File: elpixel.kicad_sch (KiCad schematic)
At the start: 5 parts, among them J1 Conn_01x02, J2 Conn_01x04, Q1 BC857, U1 MC78M05_TO252, U2 WS2811

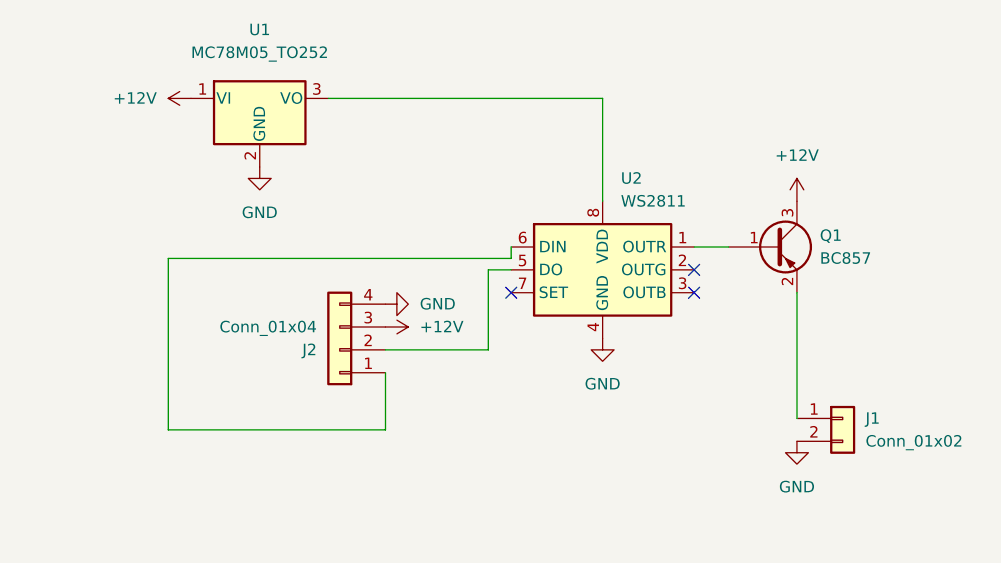
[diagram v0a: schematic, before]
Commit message: new version with different input/output pins to make the external wiring easier
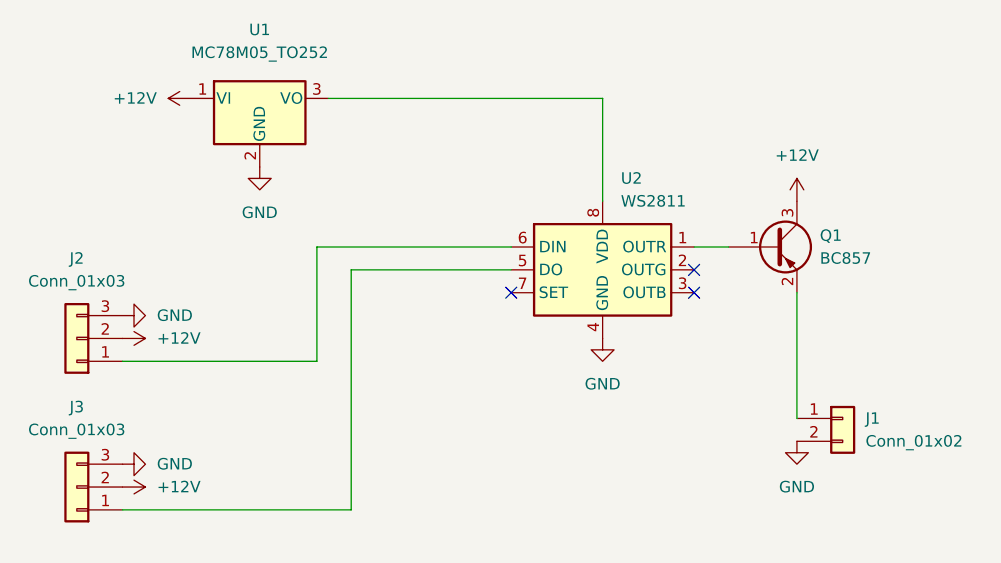
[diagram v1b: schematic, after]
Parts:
- removed J2: Conn_01x04, Connector_PinHeader_1.00mm:PinHeader_1x04_P1.00mm_Vertical, symbol Connector_Generic:Conn_01x04
- added J2, J3: Conn_01x03, Connector_PinHeader_1.00mm:PinHeader_1x03_P1.00mm_Vertical, symbol Connector_Generic:Conn_01x03
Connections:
- net +12V: now also J2.2 (Pin_2), J3.2 (Pin_2)
- net GND: now also J2.3 (Pin_3), J3.3 (Pin_3)
- net at U2.6 (DIN): now also J2.1 (Pin_1)
- net at U2.5 (DO): now also J3.1 (Pin_1)
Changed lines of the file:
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@@
   (no_connect (at 154.94 107.95))
   (no_connect (at 134.62 107.95))
+  (wire (pts (xy 134.62 105.41) (xy 116.84 105.41))
+    (stroke (width 0) (type default) (color 0 0 0 0))
+  )
+  (wire (pts (xy 116.84 105.41) (xy 116.84 132.08))
+    (stroke (width 0) (type default) (color 0 0 0 0))
+  )
   (wire (pts (xy 166.37 107.95) (xy 166.37 121.92))
     (stroke (width 0) (type default) (color 0 0 0 0))
@@
     (stroke (width 0) (type default) (color 0 0 0 0))
   )
-  (wire (pts (xy 96.52 123.19) (xy 96.52 104.14))
-    (stroke (width 0) (type default) (color 0 0 0 0))
-  )
-  (wire (pts (xy 120.65 116.84) (xy 120.65 123.19))
-    (stroke (width 0) (type default) (color 0 0 0 0))
-  )
-  (wire (pts (xy 132.08 105.41) (xy 134.62 105.41))
+  (wire (pts (xy 116.84 132.08) (xy 91.44 132.08))
     (stroke (width 0) (type default) (color 0 0 0 0))
   )
@@
     (stroke (width 0) (type default) (color 0 0 0 0))
   )
-  (wire (pts (xy 132.08 105.41) (xy 132.08 114.3))
-    (stroke (width 0) (type default) (color 0 0 0 0))
-  )
-  (wire (pts (xy 134.62 104.14) (xy 134.62 102.87))
-    (stroke (width 0) (type default) (color 0 0 0 0))
-  )
-  (wire (pts (xy 96.52 104.14) (xy 134.62 104.14))
-    (stroke (width 0) (type default) (color 0 0 0 0))
-  )
-  (wire (pts (xy 120.65 114.3) (xy 132.08 114.3))
-    (stroke (width 0) (type default) (color 0 0 0 0))
-  )
-  (wire (pts (xy 120.65 123.19) (xy 96.52 123.19))
+  (wire (pts (xy 91.44 115.57) (xy 113.03 115.57))
+    (stroke (width 0) (type default) (color 0 0 0 0))
+  )
+  (wire (pts (xy 113.03 115.57) (xy 113.03 102.87))
+    (stroke (width 0) (type default) (color 0 0 0 0))
+  )
+  (wire (pts (xy 113.03 102.87) (xy 134.62 102.87))
     (stroke (width 0) (type default) (color 0 0 0 0))
   )
@@
     (pin "3")
   )
+  (symbol (lib_id "Connector_Generic:Conn_01x03") (at 86.36 113.03 180) (unit 1)
+    (in_bom yes) (on_board yes) (fields_autoplaced)
+    (property "Reference" "J2" (id 0) (at 86.36 104.14 0))
+    (property "Value" "Conn_01x03" (id 1) (at 86.36 106.68 0))
+    (property "Footprint" "Connector_PinHeader_1.00mm:PinHeader_1x03_P1.00mm_Vertical" (id 2) (at 86.36 113.03 0)
+      (effects (font (size 1.27 1.27)) hide)
+    )
+    (property "Datasheet" "~" (id 3) (at 86.36 113.03 0)
+      (effects (font (size 1.27 1.27)) hide)
+    )
+    (pin "1")
+    (pin "2")
+    (pin "3")
+  )
   (symbol (lib_id "power:+12V") (at 99.06 86.36 90) (unit 1)
     (in_bom yes) (on_board yes) (fields_autoplaced)
@@
     )
     (property "Datasheet" "" (id 3) (at 99.06 86.36 0)
+      (effects (font (size 1.27 1.27)) hide)
+    )
+    (pin "1")
+  )
+  (symbol (lib_id "power:GND") (at 91.44 110.49 90) (unit 1)
+    (in_bom yes) (on_board yes) (fields_autoplaced)
+    (property "Reference" "#PWR0101" (id 0) (at 97.79 110.49 0)
+      (effects (font (size 1.27 1.27)) hide)
+    )
+    (property "Value" "GND" (id 1) (at 95.25 110.4899 90)
+      (effects (font (size 1.27 1.27)) (justify right))
+    )
+    (property "Footprint" "" (id 2) (at 91.44 110.49 0)
+      (effects (font (size 1.27 1.27)) hide)
+    )
+    (property "Datasheet" "" (id 3) (at 91.44 110.49 0)
+      (effects (font (size 1.27 1.27)) hide)
+    )
+    (pin "1")
+  )
+  (symbol (lib_id "power:GND") (at 91.44 127 90) (unit 1)
+    (in_bom yes) (on_board yes) (fields_autoplaced)
+    (property "Reference" "#PWR0104" (id 0) (at 97.79 127 0)
+      (effects (font (size 1.27 1.27)) hide)
+    )
+    (property "Value" "GND" (id 1) (at 95.25 126.9999 90)
+      (effects (font (size 1.27 1.27)) (justify right))
+    )
+    (property "Footprint" "" (id 2) (at 91.44 127 0)
+      (effects (font (size 1.27 1.27)) hide)
+    )
+    (property "Datasheet" "" (id 3) (at 91.44 127 0)
+      (effects (font (size 1.27 1.27)) hide)
+    )
+    (pin "1")
+  )
+  (symbol (lib_id "Connector_Generic:Conn_01x03") (at 86.36 129.54 180) (unit 1)
+    (in_bom yes) (on_board yes) (fields_autoplaced)
+    (property "Reference" "J3" (id 0) (at 86.36 120.65 0))
+    (property "Value" "Conn_01x03" (id 1) (at 86.36 123.19 0))
+    (property "Footprint" "Connector_PinHeader_1.00mm:PinHeader_1x03_P1.00mm_Vertical" (id 2) (at 86.36 129.54 0)
+      (effects (font (size 1.27 1.27)) hide)
+    )
+    (property "Datasheet" "~" (id 3) (at 86.36 129.54 0)
+      (effects (font (size 1.27 1.27)) hide)
+    )
+    (pin "1")
+    (pin "2")
+    (pin "3")
+  )
+  (symbol (lib_id "power:+12V") (at 91.44 113.03 270) (unit 1)
+    (in_bom yes) (on_board yes) (fields_autoplaced)
+    (property "Reference" "#PWR0103" (id 0) (at 87.63 113.03 0)
+      (effects (font (size 1.27 1.27)) hide)
+    )
+    (property "Value" "+12V" (id 1) (at 95.25 113.0299 90)
+      (effects (font (size 1.27 1.27)) (justify left))
+    )
+    (property "Footprint" "" (id 2) (at 91.44 113.03 0)
+      (effects (font (size 1.27 1.27)) hide)
+    )
+    (property "Datasheet" "" (id 3) (at 91.44 113.03 0)
       (effects (font (size 1.27 1.27)) hide)
     )
@@
     )
     (pin "1")
-  )
-  (symbol (lib_id "Connector_Generic:Conn_01x04") (at 115.57 114.3 180) (unit 1)
-    (in_bom yes) (on_board yes) (fields_autoplaced)
-    (property "Reference" "J2" (id 0) (at 113.03 114.3001 0)
-      (effects (font (size 1.27 1.27)) (justify left))
-    )
-    (property "Value" "Conn_01x04" (id 1) (at 113.03 111.7601 0)
-      (effects (font (size 1.27 1.27)) (justify left))
-    )
-    (property "Footprint" "Connector_PinHeader_1.00mm:PinHeader_1x04_P1.00mm_Vertical" (id 2) (at 115.57 114.3 0)
-      (effects (font (size 1.27 1.27)) hide)
-    )
-    (property "Datasheet" "~" (id 3) (at 115.57 114.3 0)
-      (effects (font (size 1.27 1.27)) hide)
-    )
-    (pin "1")
-    (pin "2")
-    (pin "3")
-    (pin "4")
   )
   (symbol (lib_id "Driver_LED:WS2811") (at 144.78 105.41 0) (unit 1)
@@
     (pin "1")
   )
-  (symbol (lib_id "power:GND") (at 120.65 109.22 90) (unit 1)
-    (in_bom yes) (on_board yes) (fields_autoplaced)
-    (property "Reference" "#PWR0101" (id 0) (at 127 109.22 0)
-      (effects (font (size 1.27 1.27)) hide)
-    )
-    (property "Value" "GND" (id 1) (at 124.46 109.2199 90)
-      (effects (font (size 1.27 1.27)) (justify right))
-    )
-    (property "Footprint" "" (id 2) (at 120.65 109.22 0)
-      (effects (font (size 1.27 1.27)) hide)
-    )
-    (property "Datasheet" "" (id 3) (at 120.65 109.22 0)
+  (symbol (lib_id "power:+12V") (at 91.44 129.54 270) (unit 1)
+    (in_bom yes) (on_board yes) (fields_autoplaced)
+    (property "Reference" "#PWR0102" (id 0) (at 87.63 129.54 0)
+      (effects (font (size 1.27 1.27)) hide)
+    )
+    (property "Value" "+12V" (id 1) (at 95.25 129.5399 90)
+      (effects (font (size 1.27 1.27)) (justify left))
+    )
+    (property "Footprint" "" (id 2) (at 91.44 129.54 0)
+      (effects (font (size 1.27 1.27)) hide)
+    )
+    (property "Datasheet" "" (id 3) (at 91.44 129.54 0)
       (effects (font (size 1.27 1.27)) hide)
     )
@@
     )
     (property "Datasheet" "" (id 3) (at 166.37 124.46 0)
-      (effects (font (size 1.27 1.27)) hide)
-    )
-    (pin "1")
-  )
-  (symbol (lib_id "power:+12V") (at 120.65 111.76 270) (unit 1)
-    (in_bom yes) (on_board yes) (fields_autoplaced)
-    (property "Reference" "#PWR0102" (id 0) (at 116.84 111.76 0)
-      (effects (font (size 1.27 1.27)) hide)
-    )
-    (property "Value" "+12V" (id 1) (at 124.46 111.7599 90)
-      (effects (font (size 1.27 1.27)) (justify left))
-    )
-    (property "Footprint" "" (id 2) (at 120.65 111.76 0)
-      (effects (font (size 1.27 1.27)) hide)
-    )
-    (property "Datasheet" "" (id 3) (at 120.65 111.76 0)
       (effects (font (size 1.27 1.27)) hide)
     )
@@
       (reference "#PWR05") (unit 1) (value "GND") (footprint "")
     )
-    (path "/a582c887-6f16-4d20-a12c-476f70d6ea35"
+    (path "/51a7453e-5942-4114-b93c-24fffffcf2da"
       (reference "#PWR0101") (unit 1) (value "GND") (footprint "")
     )
-    (path "/f3294792-4291-40c6-9d79-5617e55e671f"
+    (path "/a899f147-0456-4c4c-a26b-178ed678750a"
       (reference "#PWR0102") (unit 1) (value "+12V") (footprint "")
+    )
+    (path "/62350ef9-8386-443b-93d6-b526cf633e83"
+      (reference "#PWR0103") (unit 1) (value "+12V") (footprint "")
+    )
+    (path "/5289bc61-7716-4d1c-91dd-03b886b4760f"
+      (reference "#PWR0104") (unit 1) (value "GND") (footprint "")
     )
     (path "/f81cf28d-7f8a-45aa-8733-bbbd77ce5ecf"
       (reference "J1") (unit 1) (value "Conn_01x02") (footprint "Connector_PinHeader_1.00mm:PinHeader_1x02_P1.00mm_Vertical")
     )
-    (path "/702cc878-15d5-4e54-912a-41ec5700ad5c"
-      (reference "J2") (unit 1) (value "Conn_01x04") (footprint "Connector_PinHeader_1.00mm:PinHeader_1x04_P1.00mm_Vertical")
+    (path "/35766383-03d6-4f8b-9c16-d16020f426e2"
+      (reference "J2") (unit 1) (value "Conn_01x03") (footprint "Connector_PinHeader_1.00mm:PinHeader_1x03_P1.00mm_Vertical")
+    )
+    (path "/53789ae3-c50a-44f5-975b-fe54d0b54fab"
+      (reference "J3") (unit 1) (value "Conn_01x03") (footprint "Connector_PinHeader_1.00mm:PinHeader_1x03_P1.00mm_Vertical")
     )
     (path "/d6dc534e-6e8d-415a-9caa-ec4f0dc84478"
